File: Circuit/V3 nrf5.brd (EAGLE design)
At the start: 41 x 64.5 mm, 76 parts, among them J4 USB Micro, J7 CORTEX_DEBUG_SMD, Q1 BSS138, Q2 BSS84, U1 AL8805, U2 MCP73831, U3 BC840M, U4 3.3V/150mA, U5 AL8805, U6 AL8805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

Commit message: Trying to track down issues, cleaning up ERC.
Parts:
- removed J5: (no value), SparkFun-Connectors:1X04_1MM_RA
- moved JP3 72.1 mm to (-56.5, -58.4)
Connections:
- removed net VCC: J5.3, JP3.2, TP1.TP, U3.A7
- new net N$6: U4.4
- net 3.3V: now also TP1.TP, U3.A7; no longer J5.2
- net GND: no longer J5.1
- net VDIV: now also U3.A0; no longer U3.E4

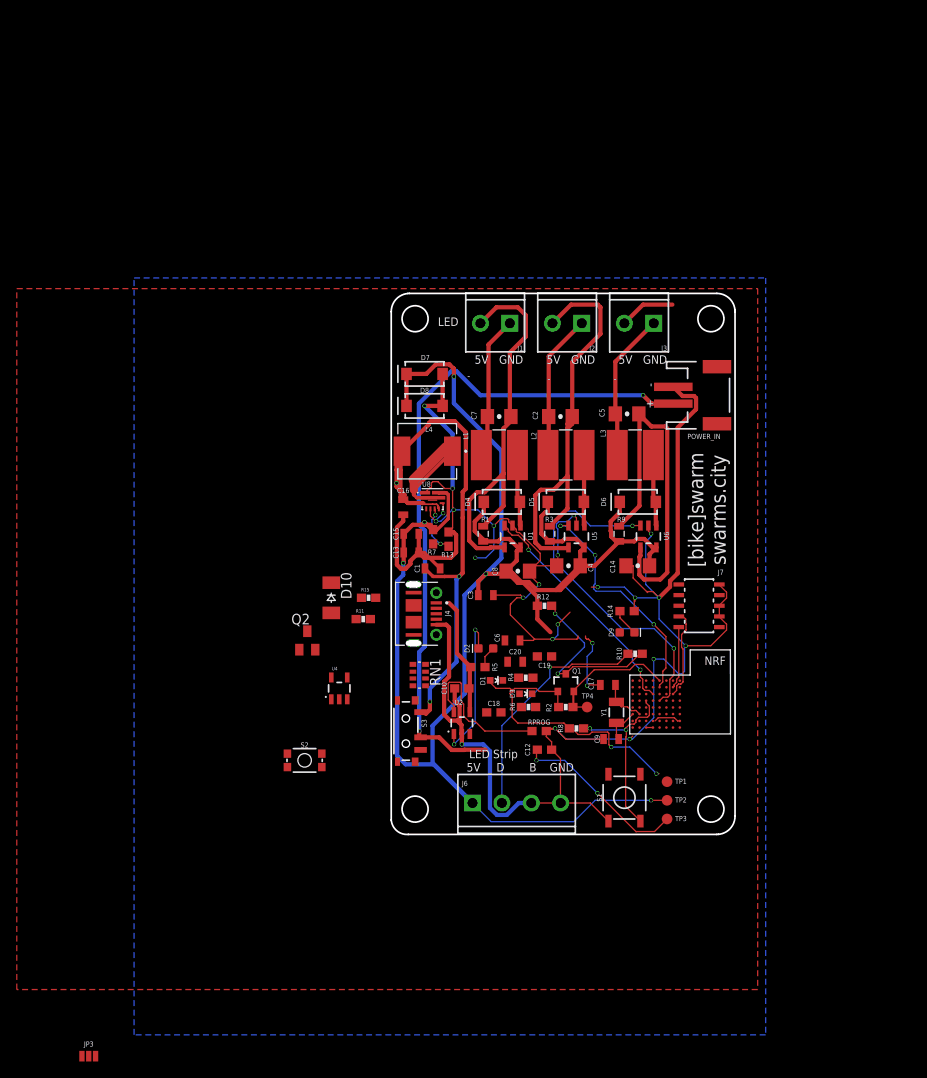
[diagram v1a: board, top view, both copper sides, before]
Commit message: updated traces
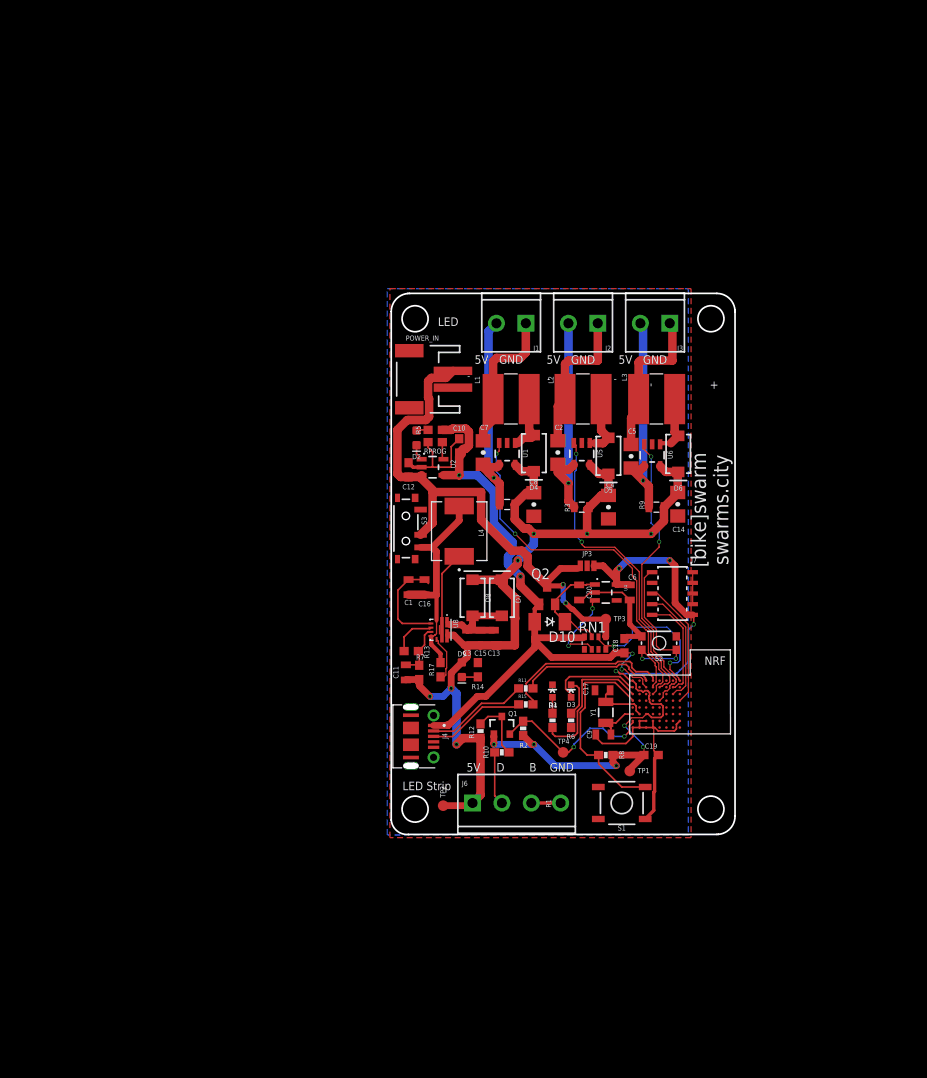
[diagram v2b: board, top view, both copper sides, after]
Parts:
- added C11: 10uF, SparkFun-Capacitors:0805
- added R17: 1M, SparkFun-Resistors:0603
- moved JP3 83.3 mm to (2.86, 0.00)
- moved S2 44.5 mm to (11.4, -9.21), turned to 180 degrees
- moved C12 37.1 mm to (-18.4, 11.4), turned to 90 degrees
- moved RPROG 36.6 mm to (-15.2, 14.7), turned to 180 degrees
- moved U4 33.7 mm to (5.08, -3.17), turned to 270 degrees
- moved POWER_IN 33.7 mm to (-16.8, 22.2), turned to 90 degrees
- moved U2 30.7 mm to (-15.6, 11.7), turned to 270 degrees
- moved Q2 29.1 mm to (-1.91, -3.49)
- moved C10 28.9 mm to (-12.4, 14.3), turned to 90 degrees
- moved R5 28.7 mm to (-15.2, 16.2), turned to 0 degrees
- moved D7 28.2 mm to (-7.30, -3.81), turned to 90 degrees
- moved TP2 26.7 mm to (-14.3, -28.6), turned to 90 degrees
- moved D2 26.4 mm to (-17.5, 15.2), turned to 270 degrees
- moved D10 26.2 mm to (-1.59, -6.67), turned to 180 degrees
- moved TP3 24.9 mm to (5.08, -6.35)
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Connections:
- net 5V: now also C11.1
- net GND: now also R17.1
- net LED_1: no longer U3.E3
- net LED_2: now also U3.B7; no longer U3.H2
- net N$9: now also C11.2
- net STRIP_3V3: now also U3.G7; no longer U3.A3
- net SWITCH_1: now also U3.D7; no longer U3.D5
- net VBATT_ON: now also R17.2, S3.1; no longer S3.3
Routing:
- net GND: track 301.2 -> 100.1 mm, vias 24 -> 0
- net 5V: track 224.3 -> 113.0 mm, vias 5 -> 7
- net VBUS: track 14.6 -> 81.4 mm, vias 0 -> 4
- net 3.3V: track 35.4 -> 84.2 mm, vias 2 -> 9
- net VBATT_ON: track 69.5 -> 27.1 mm, vias 3 -> 0
- net VBAT: track 103.5 -> 76.9 mm, vias 4 -> 2
- net OUT2+: track 51.9 -> 27.4 mm, vias 0 -> 1
- net RESET: track 0.00 -> 23.9 mm, vias 0 -> 2
- net OUT3+: track 49.7 -> 26.1 mm, vias 0 -> 1
- net N$2: track 28.5 -> 6.39 mm, vias 1 -> 0
- net OUT1+: track 48.8 -> 26.7 mm, vias 0 -> 1
- net D+: track 0.00 -> 20.5 mm
- net VDIV: track 0.00 -> 19.3 mm, vias 0 -> 2
- net LED_1: track 0.00 -> 17.3 mm
- net CTRL_CH1: track 28.1 -> 44.7 mm
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
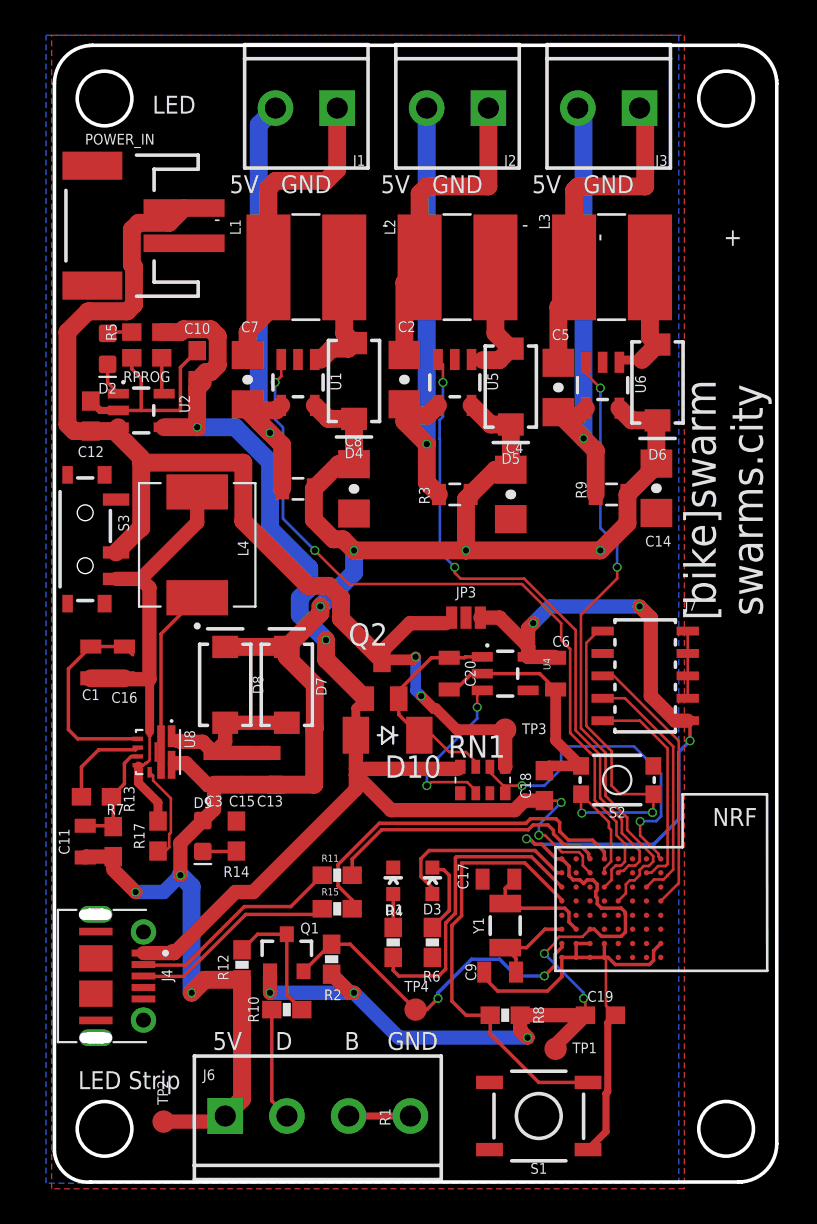
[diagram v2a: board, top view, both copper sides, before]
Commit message: traces gnd, and clean up
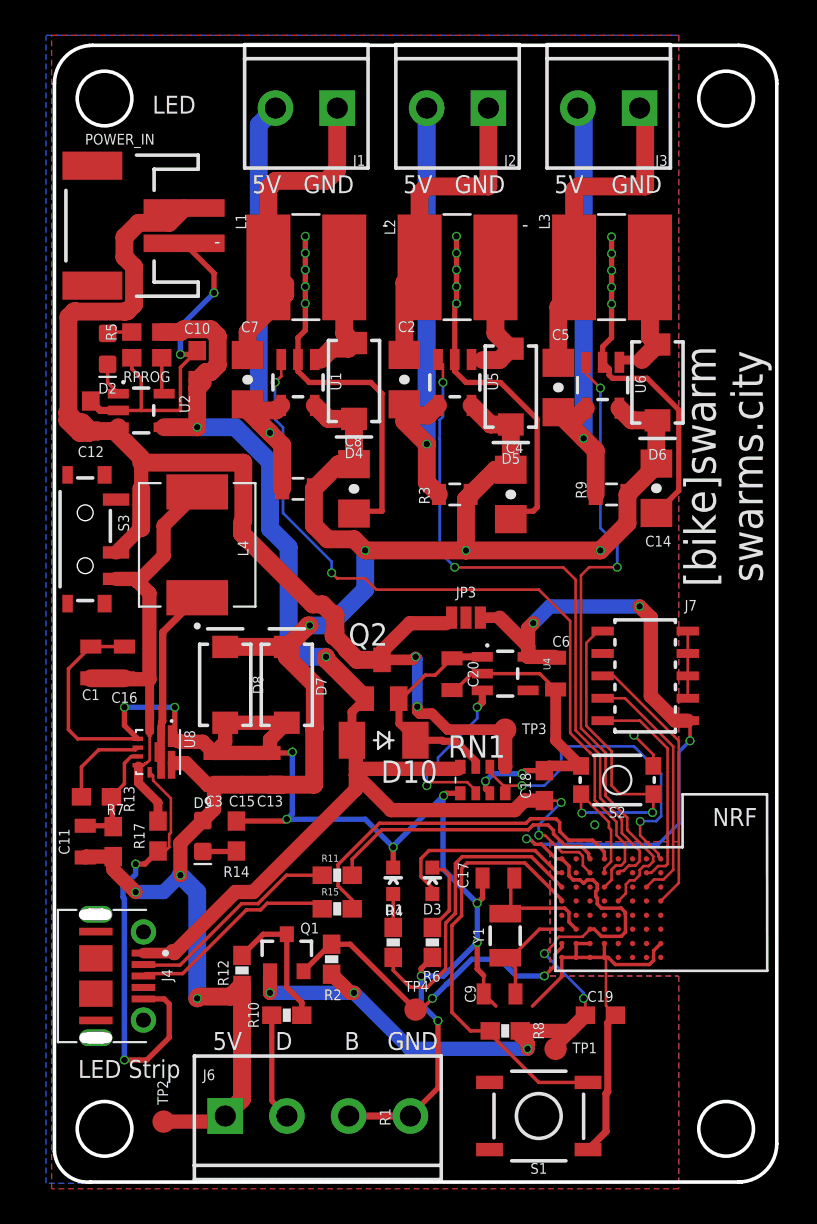
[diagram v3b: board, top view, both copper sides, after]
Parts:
- moved C9 1.24 mm to (4.76, -21.3)
- moved R8 0.89 mm to (5.08, -23.4)
- moved Y1 0.57 mm to (5.08, -18.0)
- moved D10 0.36 mm to (-1.81, -6.95)
- moved R12 0.32 mm to (-9.84, -20.0)
- moved R10 0.32 mm to (-7.30, -22.5)
- moved C20 0.16 mm to (2.06, -3.21)
- moved C17 0.06 mm to (4.70, -14.8)
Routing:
- net GND: track 100.1 -> 251.1 mm, vias 0 -> 33
- net N$3: track 9.60 -> 19.7 mm
- net VBAT: track 76.9 -> 74.3 mm
- net N$4: track 12.7 -> 14.7 mm
- net STRIP_5V: track 7.53 -> 9.29 mm
- net CTRL_CH2: track 36.9 -> 38.4 mm
- net N$9: track 7.28 -> 8.72 mm
- net 5V: track 113.0 -> 114.0 mm
- net CTRL_CH3: track 35.0 -> 35.9 mm
- net N$10: track 5.28 -> 6.17 mm
- net OUT1-: track 17.8 -> 18.6 mm
- net N$16: track 11.7 -> 12.4 mm
- net N$8: track 6.55 -> 7.20 mm
- net CTRL_CH1: track 44.7 -> 45.3 mm
- net 3.3V: track 84.2 -> 84.8 mm
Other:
- board text added: "[bike]swarm V3 12/08/2020 swarms.city"
- board text removed: "+"
- board text removed: "[bike]swarm V3 11/20/2020 swarms.city"

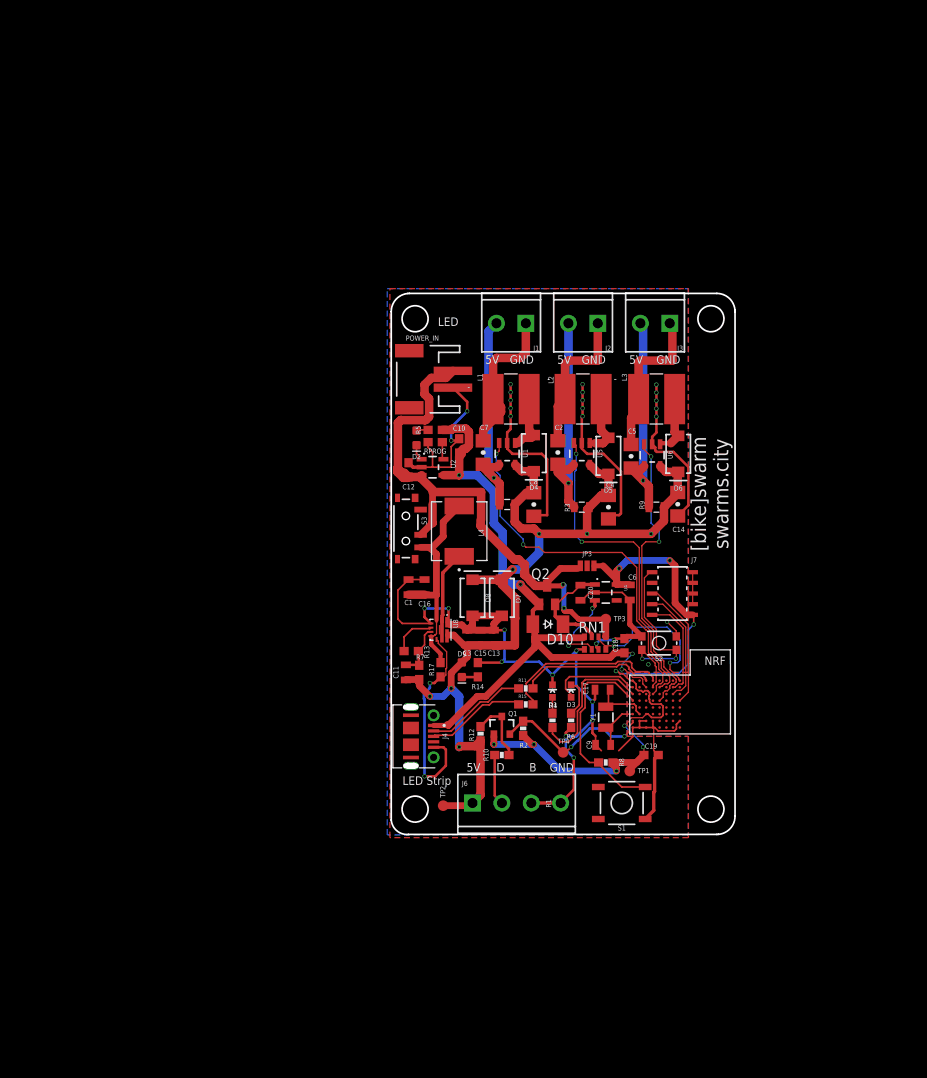
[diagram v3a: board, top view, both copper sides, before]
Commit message: updated digikey parts
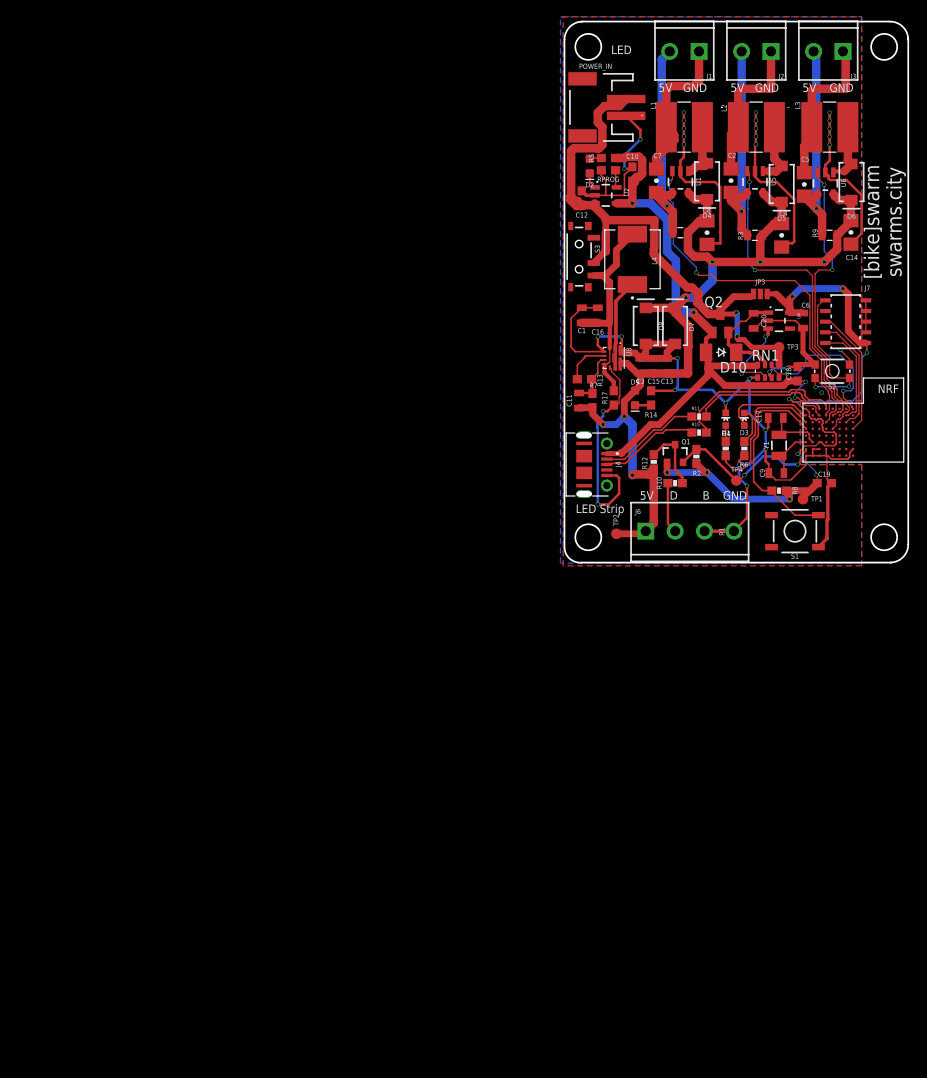
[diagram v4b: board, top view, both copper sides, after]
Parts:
- moved C14 38.4 mm to (34.3, 39.7)
- moved D9 38.4 mm to (8.57, 20.0)
- moved J1 38.4 mm to (16.2, 61.3)
- moved J2 38.4 mm to (24.8, 61.3)
- moved J3 38.4 mm to (33.3, 61.3)
- moved L1 38.4 mm to (14.4, 52.1)
- moved L2 38.4 mm to (23.0, 52.1)
- moved L3 38.4 mm to (31.8, 52.1)
- moved L4 38.4 mm to (8.26, 36.5)
- moved Q1 38.4 mm to (13.3, 13.3)
- moved R11 38.4 mm to (16.2, 17.8)
- moved R12 38.4 mm to (10.8, 12.4)
- moved R13 38.4 mm to (2.54, 22.2)
- moved R14 38.4 mm to (10.5, 20.0)
- moved R15 38.4 mm to (16.2, 15.9)
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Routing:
- net GND: track 251.1 -> 253.6 mm

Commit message: fix ERC msgs
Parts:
- moved C12 0.95 mm to (2.19, 42.9)
- moved RPROG 0.93 mm to (5.27, 46.2)
- moved U2 0.83 mm to (5.02, 43.3)
- moved R2 0.76 mm to (16.6, 13.0)
- moved Q1 0.63 mm to (14.0, 13.3)
- moved R11 0.63 mm to (16.2, 18.4)
- moved S3 0.63 mm to (1.91, 36.2)
- moved POWER_IN 0.61 mm to (4.38, 54.8)
- moved L1 0.51 mm to (14.9, 52.1)
- moved D2 0.44 mm to (3.02, 47.2)
- moved R5 0.43 mm to (5.27, 48.2)
- moved R15 0.41 mm to (16.2, 16.3)
- moved C10 0.41 mm to (8.00, 46.4)
- moved U1 0.38 mm to (14.4, 45.8)
- moved C14 0.32 mm to (34.0, 39.7)
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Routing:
- net VBAT: track 74.3 -> 79.8 mm
- net GND: track 253.6 -> 249.4 mm
- net 3.3V: track 84.8 -> 82.9 mm
- net N$2: track 6.07 -> 7.68 mm
- net VBUS: track 81.8 -> 83.4 mm
- net N$16: track 12.4 -> 13.5 mm
- net STRIP_5V: track 9.29 -> 8.35 mm
- net D+: track 20.5 -> 21.3 mm
- net OUT1-: track 18.6 -> 17.8 mm
- net SWDIO: track 12.3 -> 12.8 mm
